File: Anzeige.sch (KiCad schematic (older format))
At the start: 31 parts, among them J801 Conn_01x04, J802 Conn_01x04, U801 MCP23017_SO

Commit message: fertig zum routen
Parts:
- removed J801: Conn_01x04, Connector_PinHeader_2.54mm:PinHeader_1x04_P2.54mm_Vertical, symbol Connector_Generic:Conn_01x04
- added J801: Conn_01x05, Connector:1x04_P2.54mm_1.3OLED, symbol Connector_Generic:Conn_01x05
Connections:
- net +3V3: now also C801.2, J801.2 (Pin_2); no longer C801.1
- net GND: now also C801.1, J801.1 (Pin_1), J801.5 (Pin_5); no longer C801.2
- net SCL: now also J801.3 (Pin_3)
- net SDA: now also J801.4 (Pin_4)
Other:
- moved on the sheet: C801, C802, J802
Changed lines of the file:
@@
 L Connector_Generic:Conn_01x04 J802
 U 1 1 5F610586
-P 3400 4950
-F 0 "J802" H 3480 4942 50  0000 L CNN
-F 1 "Conn_01x04" H 3480 4851 50  0000 L CNN
-F 2 "Connector_PinHeader_2.54mm:PinHeader_1x04_P2.54mm_Vertical" H 3400 4950 50  0001 C CNN
-F 3 "~" H 3400 4950 50  0001 C CNN
-	1    3400 4950
+P 5300 5000
+F 0 "J802" H 5380 4992 50  0000 L CNN
+F 1 "Conn_01x04" H 5380 4901 50  0000 L CNN
+F 2 "Connector_PinHeader_2.54mm:PinHeader_1x04_P2.54mm_Vertical" H 5300 5000 50  0001 C CNN
+F 3 "~" H 5300 5000 50  0001 C CNN
+	1    5300 5000
 	1    0    0    -1
 $EndComp
@@
 L power:GND #PWR0809
 U 1 1 5F61077C
-P 3100 5400
-F 0 "#PWR0809" H 3100 5150 50  0001 C CNN
-F 1 "GND" H 3105 5227 50  0000 C CNN
-F 2 "" H 3100 5400 50  0001 C CNN
-F 3 "" H 3100 5400 50  0001 C CNN
-	1    3100 5400
+P 5000 5450
+F 0 "#PWR0809" H 5000 5200 50  0001 C CNN
+F 1 "GND" H 5005 5277 50  0000 C CNN
+F 2 "" H 5000 5450 50  0001 C CNN
+F 3 "" H 5000 5450 50  0001 C CNN
+	1    5000 5450
 	1    0    0    -1
 $EndComp
 Wire Wire Line
-	3200 5150 3100 5150
+	5100 5200 5000 5200
 Wire Wire Line
-	3100 5150 3100 5350
+	5000 5200 5000 5400
 $Comp
 L power:+3V3 #PWR0807
 U 1 1 5F6121E4
-P 2750 4900
-F 0 "#PWR0807" H 2750 4750 50  0001 C CNN
-F 1 "+3V3" H 2765 5073 50  0000 C CNN
-F 2 "" H 2750 4900 50  0001 C CNN
-F 3 "" H 2750 4900 50  0001 C CNN
-	1    2750 4900
+P 4650 4950
+F 0 "#PWR0807" H 4650 4800 50  0001 C CNN
+F 1 "+3V3" H 4665 5123 50  0000 C CNN
+F 2 "" H 4650 4950 50  0001 C CNN
+F 3 "" H 4650 4950 50  0001 C CNN
+	1    4650 4950
 	1    0    0    -1
 $EndComp
 Wire Wire Line
-	2750 4900 2750 5050
+	4650 4950 4650 5100
 Wire Wire Line
-	2750 5050 3200 5050
+	4650 5100 5100 5100
 $Comp
 L Device:C_Small C802
 U 1 1 5F613EA2
-P 2750 5150
-F 0 "C802" H 2842 5196 50  0000 L CNN
-F 1 "100nF" H 2842 5105 50  0000 L CNN
-F 2 "Capacitor_SMD:C_0603_1608Metric_Pad1.05x0.95mm_HandSolder" H 2750 5150 50  0001 C CNN
-F 3 "~" H 2750 5150 50  0001 C CNN
-	1    2750 5150
+P 4650 5200
+F 0 "C802" H 4742 5246 50  0000 L CNN
+F 1 "100nF" H 4742 5155 50  0000 L CNN
+F 2 "Capacitor_SMD:C_0603_1608Metric_Pad1.05x0.95mm_HandSolder" H 4650 5200 50  0001 C CNN
+F 3 "~" H 4650 5200 50  0001 C CNN
+	1    4650 5200
 	1    0    0    -1
 $EndComp
-Connection ~ 2750 5050
+Connection ~ 4650 5100
 Wire Wire Line
-	2750 5250 2750 5350
+	4650 5300 4650 5400
 Wire Wire Line
-	2750 5350 3100 5350
-Connection ~ 3100 5350
+	4650 5400 5000 5400
+Connection ~ 5000 5400
 Wire Wire Line
-	3100 5350 3100 5400
-Text GLabel 3050 4850 0    50   Input ~ 0
+	5000 5400 5000 5450
+Text GLabel 4950 4900 0    50   Input ~ 0
 SDA
 Wire Wire Line
-	3200 4850 3050 4850
-Text GLabel 3050 4950 0    50   Input ~ 0
+	5100 4900 4950 4900
+Text GLabel 4950 5000 0    50   Input ~ 0
 SCL
 Wire Wire Line
-	3200 4950 3050 4950
-$Comp
-L Connector_Generic:Conn_01x04 J801
-U 1 1 5F61FAF7
-P 1850 4950
-F 0 "J801" H 1930 4942 50  0000 L CNN
-F 1 "Conn_01x04" H 1930 4851 50  0000 L CNN
-F 2 "Connector_PinHeader_2.54mm:PinHeader_1x04_P2.54mm_Vertical" H 1850 4950 50  0001 C CNN
-F 3 "~" H 1850 4950 50  0001 C CNN
-	1    1850 4950
-	1    0    0    -1
-$EndComp
+	5100 5000 4950 5000
 $Comp
 L power:GND #PWR0802
@@
 	1    0    0    -1
 $EndComp
-Wire Wire Line
-	1650 5150 1550 5150
-Wire Wire Line
-	1550 5150 1550 5350
 $Comp
 L power:+3V3 #PWR0801
 U 1 1 5F61FB06
-P 1200 4900
-F 0 "#PWR0801" H 1200 4750 50  0001 C CNN
-F 1 "+3V3" H 1215 5073 50  0000 C CNN
-F 2 "" H 1200 4900 50  0001 C CNN
-F 3 "" H 1200 4900 50  0001 C CNN
-	1    1200 4900
+P 1250 4950
+F 0 "#PWR0801" H 1250 4800 50  0001 C CNN
+F 1 "+3V3" V 1250 5200 50  0000 C CNN
+F 2 "" H 1250 4950 50  0001 C CNN
+F 3 "" H 1250 4950 50  0001 C CNN
+	1    1250 4950
+	0    -1   -1   0
+$EndComp
+$Comp
+L Device:C_Small C801
+U 1 1 5F61FB0E
+P 1500 4750
+F 0 "C801" H 1592 4796 50  0000 L CNN
+F 1 "100nF" H 1592 4705 50  0000 L CNN
+F 2 "Capacitor_SMD:C_0603_1608Metric_Pad1.05x0.95mm_HandSolder" H 1500 4750 50  0001 C CNN
+F 3 "~" H 1500 4750 50  0001 C CNN
+	1    1500 4750
+	0    -1   -1   0
+$EndComp
+Text GLabel 1450 5150 0    50   Input ~ 0
+SDA
+Wire Wire Line
+	1650 4850 1400 4850
+Text GLabel 1450 5050 0    50   Input ~ 0
+SCL
+Wire Wire Line
+	1650 4950 1600 4950
+Text Notes 800  4650 0    50   ~ 0
+OLED Display
+Text Notes 4950 4750 0    50   ~ 0
+I2C-Sensor
+$Comp
+L Connector_Generic:Conn_01x05 J801
+U 1 1 5E98BB32
+P 1850 5050
+F 0 "J801" H 1930 5092 50  0000 L CNN
+F 1 "Conn_01x05" H 1930 5001 50  0000 L CNN
+F 2 "Connector:1x04_P2.54mm_1.3OLED" H 1850 5050 50  0001 C CNN
+F 3 "~" H 1850 5050 50  0001 C CNN
+	1    1850 5050
 	1    0    0    -1
 $EndComp
 Wire Wire Line
-	1200 4900 1200 5050
+	1650 5250 1550 5250
 Wire Wire Line
-	1200 5050 1650 5050
+	1550 5250 1550 5400
 $Comp
-L Device:C_Small C801
-U 1 1 5F61FB0E
-P 1200 5150
-F 0 "C801" H 1292 5196 50  0000 L CNN
-F 1 "100nF" H 1292 5105 50  0000 L CNN
-F 2 "Capacitor_SMD:C_0603_1608Metric_Pad1.05x0.95mm_HandSolder" H 1200 5150 50  0001 C CNN
-F 3 "~" H 1200 5150 50  0001 C CNN
-	1    1200 5150
-	1    0    0    -1
+L power:GND #PWR0192
+U 1 1 5E99C353
+P 1300 4850
+F 0 "#PWR0192" H 1300 4600 50  0001 C CNN
+F 1 "GND" V 1300 4600 50  0000 C CNN
+F 2 "" H 1300 4850 50  0001 C CNN
+F 3 "" H 1300 4850 50  0001 C CNN
+	1    1300 4850
+	0    1    1    0
 $EndComp
-Connection ~ 1200 5050
 Wire Wire Line
-	1200 5250 1200 5350
+	1650 5150 1450 5150
 Wire Wire Line
-	1200 5350 1550 5350
-Connection ~ 1550 5350
+	1650 5050 1450 5050
 Wire Wire Line
-	1550 5350 1550 5400
-Text GLabel 1500 4850 0    50   Input ~ 0
-SDA
+	1400 4750 1400 4850
+Connection ~ 1400 4850
 Wire Wire Line
-	1650 4850 1500 4850
-Text GLabel 1500 4950 0    50   Input ~ 0
-SCL
+	1400 4850 1300 4850
 Wire Wire Line
-	1650 4950 1500 4950
-Text Notes 1400 4700 0    50   ~ 0
-OLED Display
-Text Notes 3050 4700 0    50   ~ 0
-I2C-Sensor
+	1600 4750 1600 4950
+Connection ~ 1600 4950
+Wire Wire Line
+	1600 4950 1250 4950
 $EndSCHEMATC

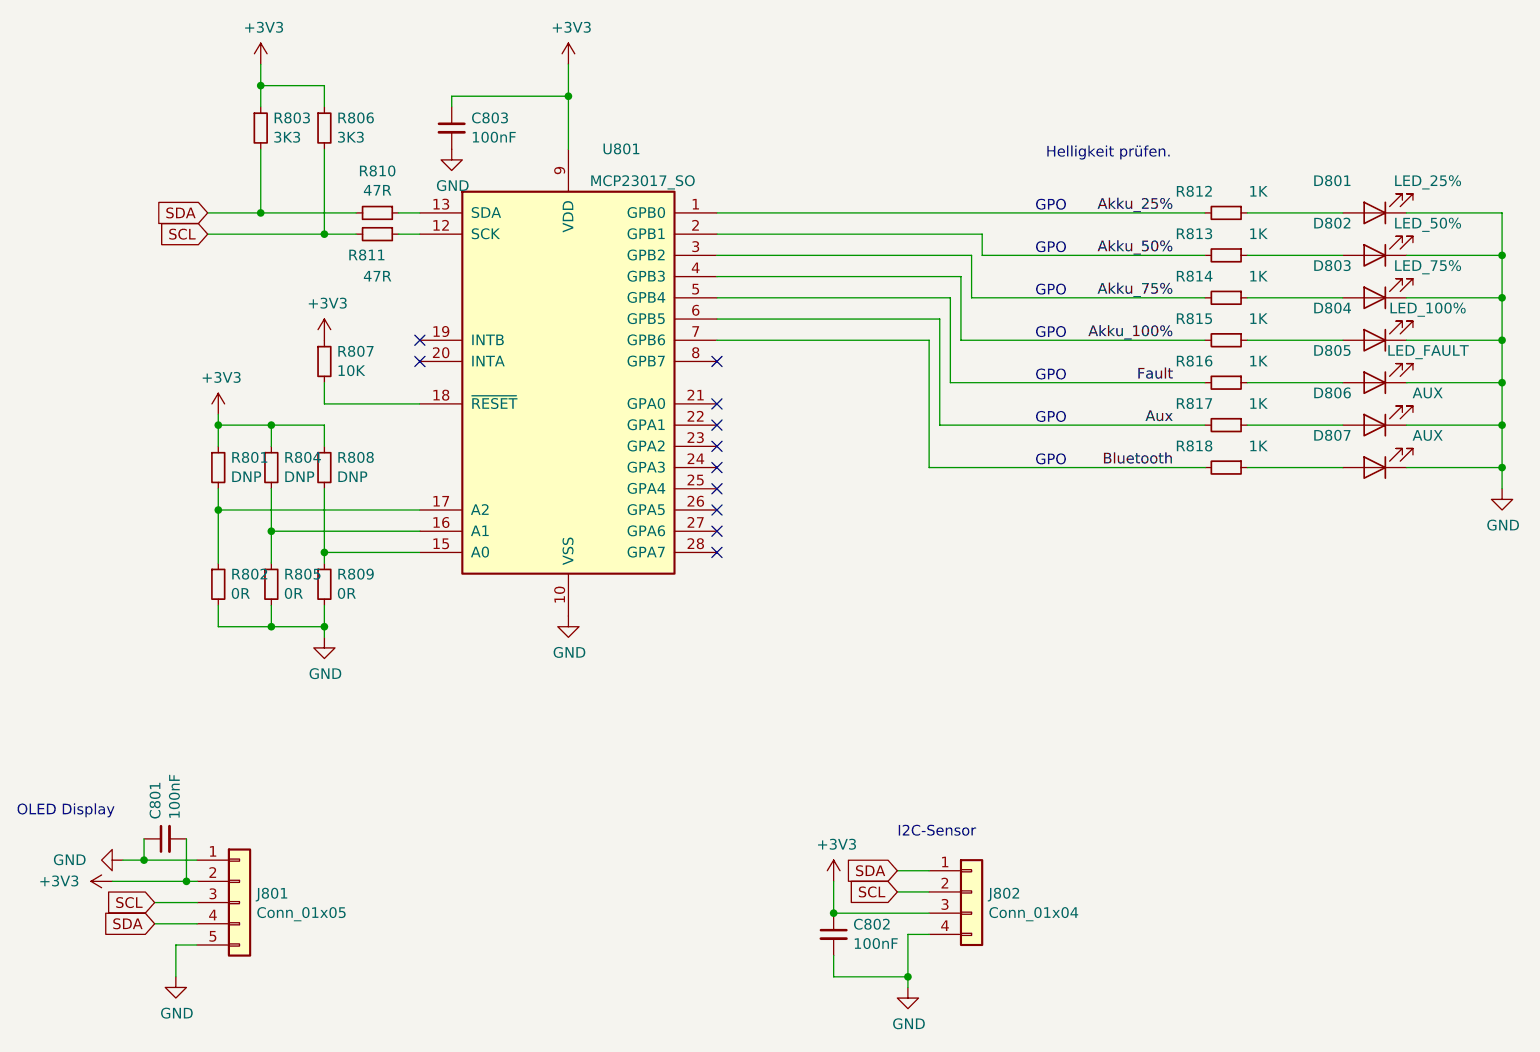
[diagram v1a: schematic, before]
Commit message: Folienkondensatoren SMD gegen THT ausgetauscht. Kleine Fehler korrigiert
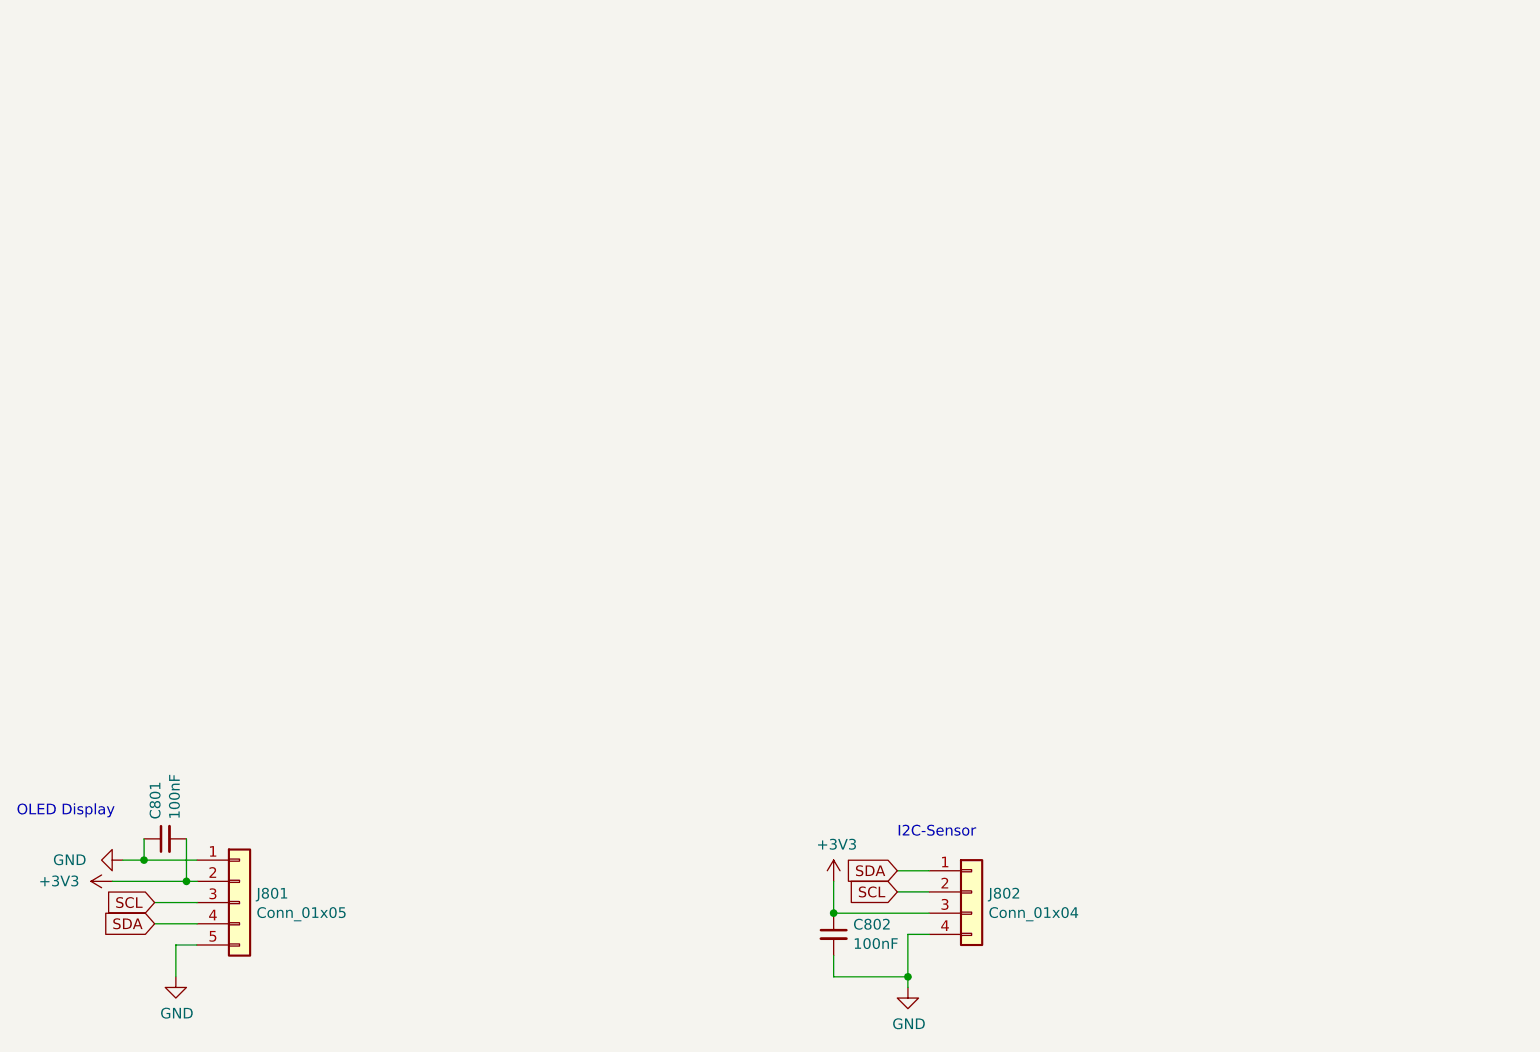
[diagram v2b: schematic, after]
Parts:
- removed C803: 100nF, Capacitor_SMD:C_0603_1608Metric_Pad1.05x0.95mm_HandSolder, symbol Device:C_Small
- removed D801: LED_25%, LED_THT:LED_D5.0mm, symbol Device:LED
- removed D802: LED_50%, LED_THT:LED_D5.0mm, symbol Device:LED
- removed D803: LED_75%, LED_THT:LED_D5.0mm, symbol Device:LED
- removed D804: LED_100%, LED_THT:LED_D5.0mm, symbol Device:LED
- removed D805: LED_FAULT, LED_THT:LED_D5.0mm, symbol Device:LED
- removed D806, D807: AUX, LED_THT:LED_D5.0mm, symbol Device:LED
- removed R801, R804, R808: DNP, Resistor_SMD:R_0603_1608Metric_Pad1.05x0.95mm_HandSolder, symbol Device:R_Small
- removed R802, R805, R809: 0R, Resistor_SMD:R_0603_1608Metric_Pad1.05x0.95mm_HandSolder, symbol Device:R_Small
- removed R803, R806: 3K3, Resistor_SMD:R_0603_1608Metric_Pad1.05x0.95mm_HandSolder, symbol Device:R_Small
- removed R807: 10K, Resistor_SMD:R_0603_1608Metric_Pad1.05x0.95mm_HandSolder, symbol Device:R_Small
- removed R810, R811: 47R, Resistor_SMD:R_0603_1608Metric_Pad1.05x0.95mm_HandSolder, symbol Device:R_Small
- removed R812, R813, R814, R815, R816, R817, R818: 1K, Resistor_SMD:R_0603_1608Metric_Pad1.05x0.95mm_HandSolder, symbol Device:R_Small
- removed U801: MCP23017_SO, Package_SO:SOIC-28W_7.5x17.9mm_P1.27mm, symbol Interface_Expansion:MCP23017_SO
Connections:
- no-connect marks 11 -> 0
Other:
- note removed: "GPO"
- note removed: "Helligkeit prüfen."
